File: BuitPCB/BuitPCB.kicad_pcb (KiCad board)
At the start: 2 copper layers, 100 x 100 mm, 46 parts, among them J1 DIN-5_180degree, J10 Conn_01x06, J11 Conn_01x04, J12 Conn_01x04, J13 Conn_01x02, J15 Conn_01x04, J16 Conn_01x04, J2 DIN-5_180degree, J3 USB_A, J4 AudioJack3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

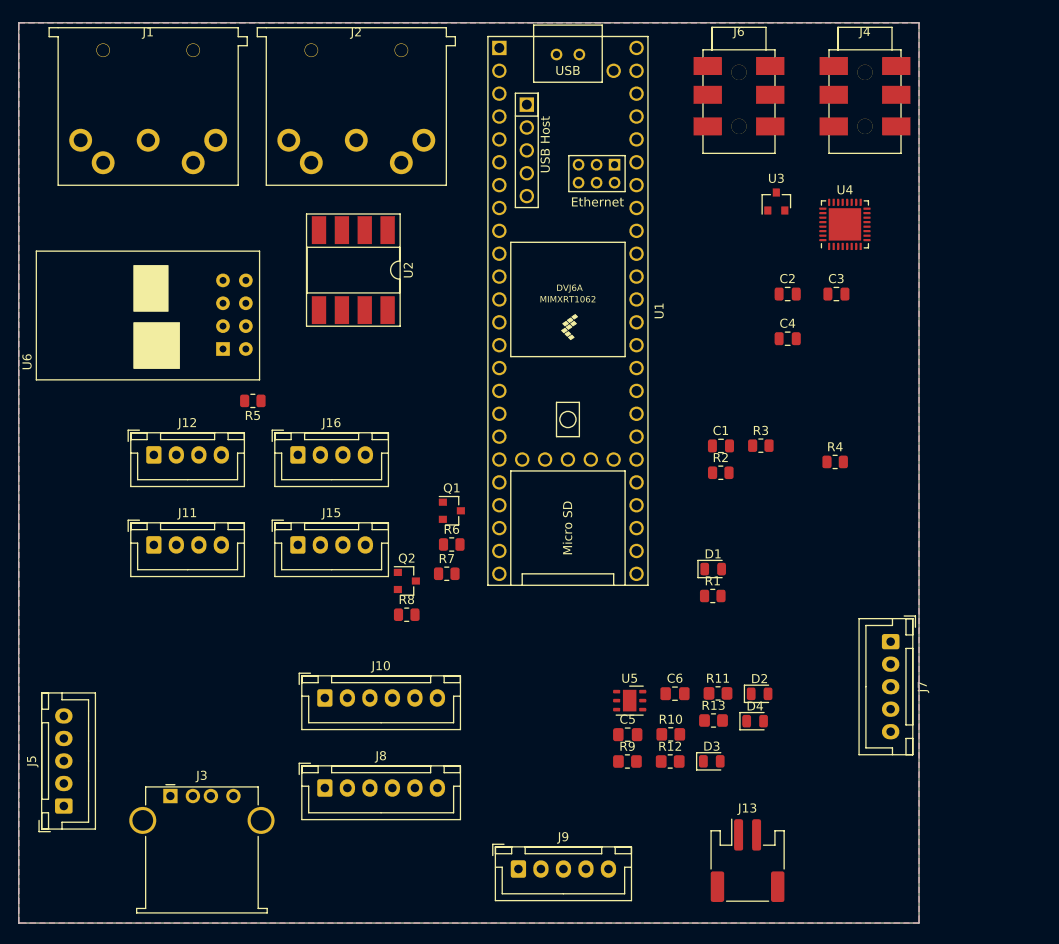
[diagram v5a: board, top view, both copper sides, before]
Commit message: Updated to almost every component and started routing
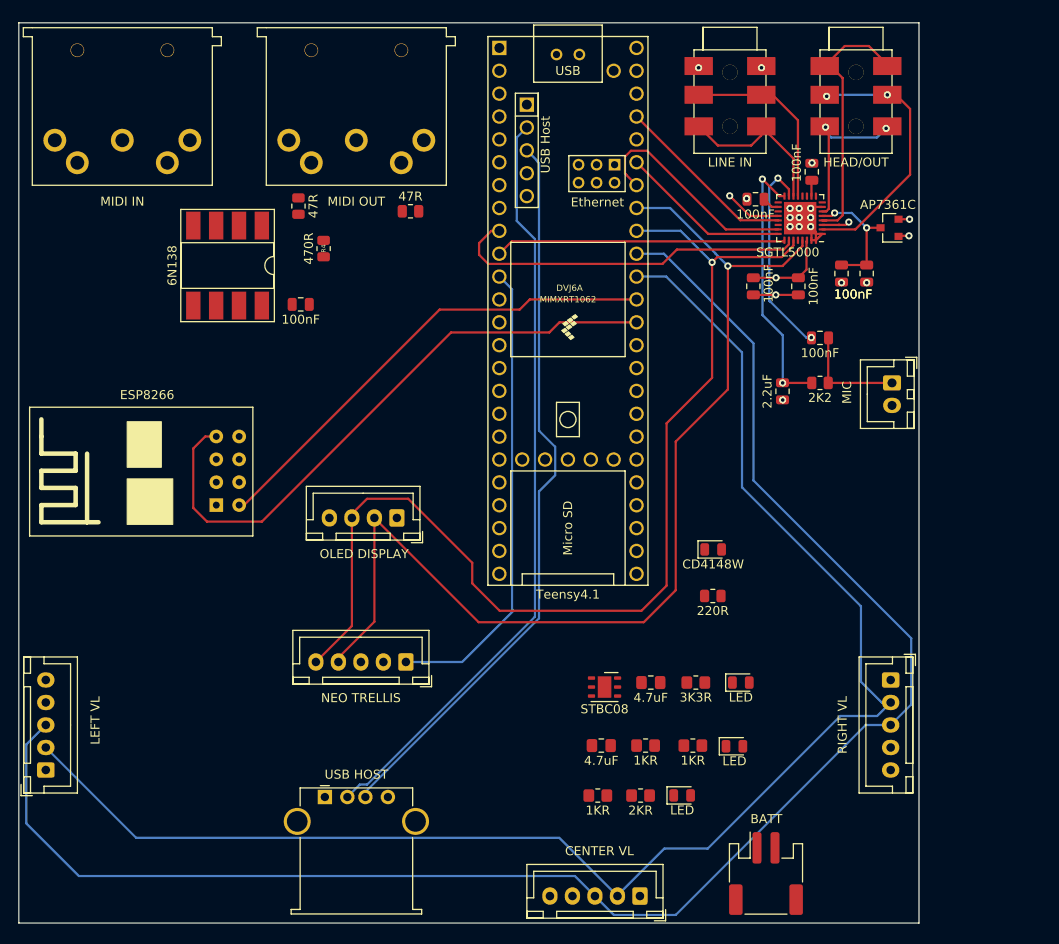
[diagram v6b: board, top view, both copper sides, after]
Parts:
- removed J10: Conn_01x06, Connector_JST:JST_XH_B6B-XH-A_1x06_P2.50mm_Vertical
- removed J15, J16: Conn_01x04, Connector_JST:JST_XH_B4B-XH-A_1x04_P2.50mm_Vertical
- removed Q1, Q2: BSS138, Package_TO_SOT_SMD:SOT-23
- removed R5, R6, R7, R8: 10K, Resistor_SMD:R_0805_2012Metric
- added C10: 100nF, Capacitor_SMD:C_0805_2012Metric, F.Cu at (189.0, 85.0)
- added C11: 2.2uF, Capacitor_SMD:C_0805_2012Metric, F.Cu at (184.8, 90.9)
- added C7: 100nF, Capacitor_SMD:C_0805_2012Metric, F.Cu at (181.6, 79.3)
- added C8: 100nF, Capacitor_SMD:C_0805_2012Metric, F.Cu at (188.1, 66.5)
- added C9: 100nF, Capacitor_SMD:C_0805_2012Metric, F.Cu at (181.8, 69.6)
- added R14: 2K2, Resistor_SMD:R_0805_2012Metric, F.Cu at (189.0, 90.0)
- C1: value C -> 100nF
- J1: value DIN-5_180degree -> MIDI IN
- J11: value Conn_01x04 -> OLED DISPLAY
- J12: value Conn_01x04 -> NEO TRELLIS; footprint Connector_JST:JST_XH_B4B-XH-A_1x04_P2.50mm_Vertical -> Connector_JST:JST_XH_B5B-XH-A_1x05_P2.50mm_Vertical
- J13: value Conn_01x02 -> BATT
- J2: value DIN-5_180degree -> MIDI OUT
- J3: value USB_A -> USB HOST
- J4: value AudioJack3 -> LINE IN
- J5: value LEFT SENS -> LEFT VL
- J6: value AudioJack3 -> HEAD/OUT
- J7: value RIGHT SENS -> RIGHT VL
- J8: value Conn_01x06 -> MIC; footprint Connector_JST:JST_XH_B6B-XH-A_1x06_P2.50mm_Vertical -> Connector_JST:JST_XH_B2B-XH-A_1x02_P2.50mm_Vertical
- J9: value CENTER SENS -> CENTER VL
- U3: value AP7361C-33E -> AP7361C
- U4: value SGTL5000XNAA3 -> SGTL5000
- U6: value ESP82SerialTransc -> ESP8266
- moved J8 77.4 mm to (197.0, 90.0), turned to 270 degrees
- moved R4 61.6 mm to (133.9, 75.1), turned to 270 degrees
- moved R2 55.5 mm to (131.1, 70.4), turned to 90 degrees
- moved C1 49.3 mm to (131.3, 81.3)
- moved R3 46.8 mm to (143.5, 70.9), turned to 180 degrees
- moved J12 36.2 mm to (143.0, 121.0), turned to 180 degrees
- moved J11 27.2 mm to (142.0, 105.0), turned to 180 degrees
- moved U6 17.4 mm to (126.0, 107.0)
- moved J3 17.2 mm to (134.0, 136.0)
- moved J4 15.0 mm to (179.0, 53.0)
- moved U2 14.0 mm to (123.2, 77.0)
- moved J9 13.8 mm to (169.0, 147.0), turned to 180 degrees
- moved J6 13.0 mm to (193.0, 53.0)
- moved U3 12.9 mm to (196.7, 72.8), turned to 180 degrees
- moved C2 6.40 mm to (191.4, 77.9), turned to 270 degrees
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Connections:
- C4 pad 1: Net-(C4-Pad1) -> GND
- C4 pad 2: Net-(C4-Pad2) -> +3V3
- J12 pad 1: +3V3 -> TRELLIS_INT_PIN
- J12 pad 2: I2C_SCL_3V3 -> +3V3
- J12 pad 3: I2C_SDA_3V3 -> GND
- J12 pad 4: GND -> I2C_SCL_3V3
- J8 pad 1: +3V3 -> Net-(C10-Pad2)
- J8 pad 2: SPI_MISO -> GND
- U1 pad 11: Net-(U1-Pad11) -> TRELLIS_INT_PIN
- U4 pad 15: Net-(U4-Pad15) -> MIC
- U4 pad 16: Net-(U4-Pad16) -> MIC_BIAS
- U4 pad 20: Net-(U4-Pad20) -> +3V3
- U4 pad 30: Net-(U4-Pad30) -> +3V3
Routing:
- net SENS_I2C_SDA: track 0.00 -> 188.5 mm
- net SENS_I2C_SCL: track 0.00 -> 171.1 mm
- net I2C_SDA_3V3: track 0.00 -> 119.7 mm, vias 0 -> 1
- net I2C_SCL_3V3: track 0.00 -> 118.5 mm, vias 0 -> 1
- net USB_HOST_D-: track 0.00 -> 84.8 mm
- net USB_HOST_D+: track 0.00 -> 81.9 mm
- net ESP8266_UART_RX: track 0.00 -> 68.8 mm
- net ESP8266_UART_TX: track 0.00 -> 53.6 mm
- net TRELLIS_INT_PIN: track 0.00 -> 52.1 mm
- net I2S_DIN: track 0.00 -> 40.3 mm
- net I2S_DOUT: track 0.00 -> 32.3 mm
- net MIC_BIAS: track 0.00 -> 30.3 mm, vias 0 -> 2
- net HP_GND: track 0.00 -> 29.6 mm
- net HP_R: track 0.00 -> 29.6 mm, vias 0 -> 2
- net I2S_LRCLK: track 0.00 -> 24.6 mm
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- added copper zone on In2.Cu, net +3V3
- added copper zone on In1.Cu, net GND
- removed copper zone on B.Cu, net GND
- removed copper zone on F.Cu, net GND
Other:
- copper layers 2 -> 4

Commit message: Added drills on pcb
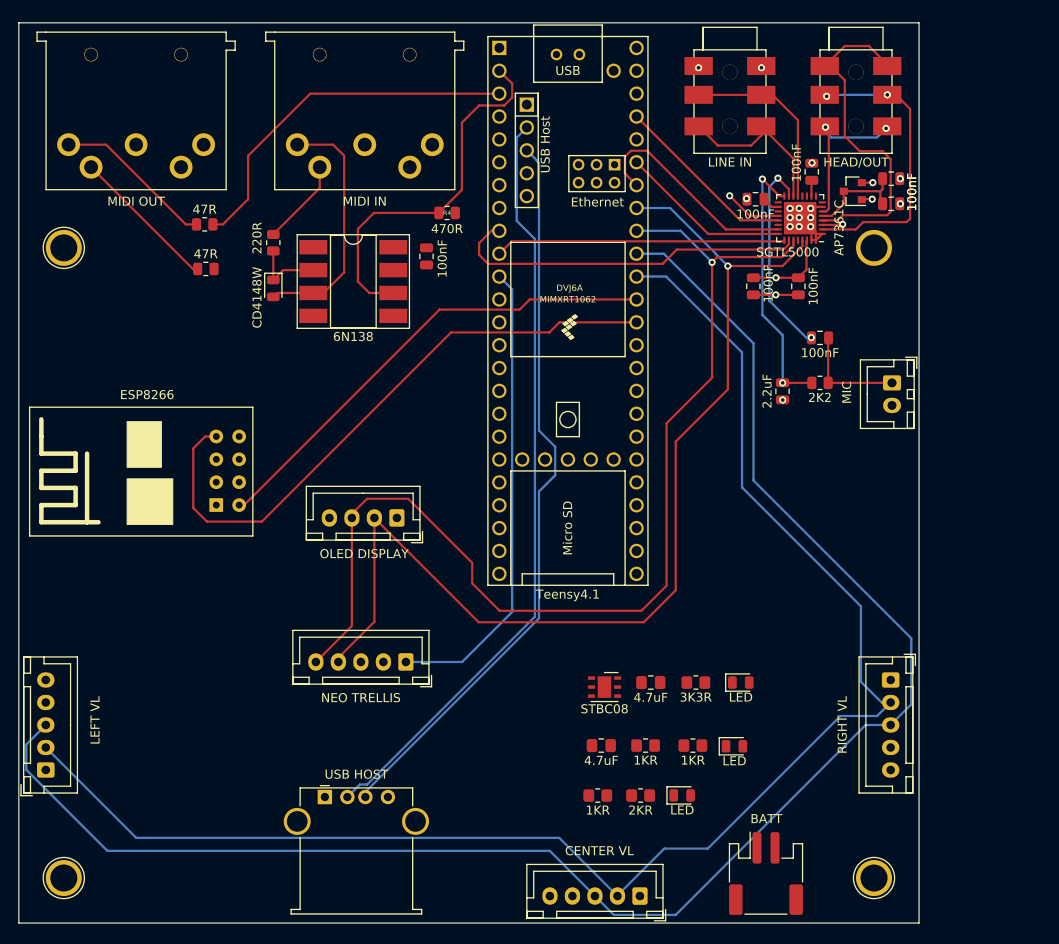
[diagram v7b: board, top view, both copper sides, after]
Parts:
- added ?: , , F.Cu at (195.0, 75.0)
- added REF**: TestPoint_Plated_Hole_D3.0mm, TestPoint:TestPoint_Plated_Hole_D3.0mm, F.Cu at (195.0, 145.0)
- added REF**: TestPoint_Plated_Hole_D3.0mm, TestPoint:TestPoint_Plated_Hole_D3.0mm, F.Cu at (105.0, 145.0)
- added REF**: TestPoint_Plated_Hole_D3.0mm, TestPoint:TestPoint_Plated_Hole_D3.0mm, F.Cu at (105.0, 75.0)
- moved R1 62.6 mm to (128.3, 74.4), turned to 90 degrees
- moved D1 56.8 mm to (128.3, 79.5), turned to -90 degrees
- moved J1 26.9 mm to (138.4, 51.0)
- moved J2 24.5 mm to (113.0, 51.0)
- moved R3 22.9 mm to (120.7, 72.4)
- moved C1 15.0 mm to (145.3, 75.9), turned to -90 degrees
- moved R4 14.3 mm to (147.6, 71.1), turned to 180 degrees
- moved U2 14.1 mm to (137.2, 78.7), turned to 0 degrees
- moved R2 12.4 mm to (120.8, 77.3), turned to 180 degrees
- moved C3 10.9 mm to (196.9, 67.3), turned to 0 degrees
- moved C2 9.51 mm to (196.9, 70.1), turned to 0 degrees
- moved U3 5.76 mm to (192.6, 68.7)
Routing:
- net MIDI_IN: track 0.00 -> 41.4 mm
- net MIDI_OUT: track 0.00 -> 40.7 mm
- net Net-(D1-Pad2): track 0.00 -> 27.7 mm
- net Net-(J2-Pad5): track 0.00 -> 17.9 mm
- net Net-(J2-Pad4): track 0.00 -> 16.5 mm
- net Net-(J1-Pad4): track 0.00 -> 9.61 mm
- net HP_GND: track 29.6 -> 38.4 mm
- net Net-(D1-Pad1): track 0.00 -> 8.13 mm
- net SENS_I2C_SDA: track 188.5 -> 185.0 mm
- net HP_R: track 29.6 -> 32.4 mm
- net VDDA: track 14.2 -> 11.4 mm, vias 2 -> 0
- net GND: track 18.8 -> 17.5 mm
- removed copper zone on In2.Cu, net +3V3
- removed copper zone on In1.Cu, net GND
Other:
- net class Default removed

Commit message: Updated almost to final 0.1 version
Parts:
- removed D2, D3, D4: LED, LED_SMD:LED_0805_2012Metric
- removed J13: BATT, Connector_JST:JST_PH_S2B-PH-SM4-TB_1x02-1MP_P2.00mm_Horizontal
- removed R10, R13, R9: 1KR, Resistor_SMD:R_0805_2012Metric_Pad1.20x1.40mm_HandSolder
- removed R11: 3K3R, Resistor_SMD:R_0805_2012Metric_Pad1.20x1.40mm_HandSolder
- removed R12: 2KR, Resistor_SMD:R_0805_2012Metric_Pad1.20x1.40mm_HandSolder
- removed the REF** at (195.0, 145.0)
- removed the REF** at (105.0, 75.0)
- removed U5: STBC08, Package_DFN_QFN:DFN-6-1EP_3x3mm_P1mm_EP1.5x2.4mm
- added ?: , , F.Cu at (105.0, 75.0)
- added ?: , , F.Cu at (195.0, 145.0)
- added C12: 100nF, Capacitor_SMD:C_0805_2012Metric, F.Cu at (146.4, 78.3)
- added J10: ROTARY CLICK, Connector_JST:JST_XH_B5B-XH-A_1x05_P2.50mm_Vertical, F.Cu at (133.3, 92.8)
- added R5: 3K3, Resistor_SMD:R_0805_2012Metric, F.Cu at (177.6, 92.9)
- added R6: 3K3, Resistor_SMD:R_0805_2012Metric, F.Cu at (175.5, 90.1)
- added R7: 3K3, Resistor_SMD:R_0805_2012Metric, F.Cu at (179.1, 99.4)
- added R8: 3K3, Resistor_SMD:R_0805_2012Metric, F.Cu at (182.8, 99.4)
- C5, C6: value 4.7uF -> 100nF; footprint Capacitor_SMD:C_0805_2012Metric_Pad1.18x1.45mm_HandSolder -> Capacitor_SMD:C_0805_2012Metric
- D1: value CD4148W -> 1N4148
- moved C6 53.9 mm to (146.4, 74.9), turned to 180 degrees
- moved C5 52.0 mm to (146.4, 81.6), turned to 180 degrees
- moved U6 6.85 mm to (125.7, 100.2)
- moved C1 4.59 mm to (142.6, 72.2), turned to 0 degrees
- moved U1 0.14 mm to (160.9, 82.1)
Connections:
- net USB_HOST_D+ renamed USB_HOST_P
- net USB_HOST_D- renamed USB_HOST_N
- C1 pad 1: +5V -> V_USB
- C5 pad 1: V_USB -> GND
- C5 pad 2: GND -> V_USB
- C6 pad 1: V_BAT -> GND
- C6 pad 2: GND -> V_USB
- J1 pad 1: Net-(J1-Pad1) -> unconnected-(J1-Pad1)
- J1 pad 2: Net-(J1-Pad2) -> unconnected-(J1-Pad2)
- J1 pad 3: Net-(J1-Pad3) -> unconnected-(J1-Pad3)
- J2 pad 1: Net-(J2-Pad1) -> unconnected-(J2-Pad1)
- J2 pad 2: Net-(J2-Pad2) -> unconnected-(J2-Pad2)
- J2 pad 3: Net-(J2-Pad3) -> unconnected-(J2-Pad3)
- J3 pad 1: Net-(J3-Pad1) -> USB_HOST_5V
- U1 pad 12: Net-(U1-Pad12) -> ROT_CLICK_SW
- U1 pad 13: Net-(U1-Pad13) -> ROT_CLICK_DT
- U1 pad 14: Net-(U1-Pad14) -> ROT_CLICK_CLK
- U1 pad 16: Net-(U1-Pad16) -> unconnected-(U1-Pad16)
- U1 pad 17: Net-(U1-Pad17) -> unconnected-(U1-Pad17)
- U1 pad 18: Net-(U1-Pad18) -> unconnected-(U1-Pad18)
- U1 pad 19: Net-(U1-Pad19) -> unconnected-(U1-Pad19)
- U1 pad 20: Net-(U1-Pad20) -> unconnected-(U1-Pad20)
- U1 pad 21: Net-(U1-Pad21) -> unconnected-(U1-Pad21)
- U1 pad 22: Net-(U1-Pad22) -> unconnected-(U1-Pad22)
- U1 pad 23: Net-(U1-Pad23) -> unconnected-(U1-Pad23)
- U1 pad 24: Net-(U1-Pad24) -> unconnected-(U1-Pad24)
- U1 pad 25: Net-(U1-Pad25) -> unconnected-(U1-Pad25)
- U1 pad 26: Net-(U1-Pad26) -> unconnected-(U1-Pad26)
- U1 pad 27: Net-(U1-Pad27) -> unconnected-(U1-Pad27)
- U1 pad 28: Net-(U1-Pad28) -> unconnected-(U1-Pad28)
- U1 pad 29: Net-(U1-Pad29) -> unconnected-(U1-Pad29)
- U1 pad 30: Net-(U1-Pad30) -> unconnected-(U1-Pad30)
- U1 pad 31: Net-(U1-Pad31) -> unconnected-(U1-Pad31)
- U1 pad 32: Net-(U1-Pad32) -> unconnected-(U1-Pad32)
- U1 pad 33: Net-(U1-Pad33) -> unconnected-(U1-Pad33)
- U1 pad 35: Net-(U1-Pad35) -> unconnected-(U1-Pad35)
- U1 pad 44: Net-(U1-Pad44) -> unconnected-(U1-Pad44)
- U1 pad 46: Net-(U1-Pad46) -> +3V3
- U1 pad 48: Net-(U1-Pad48) -> V_USB
- U1 pad 49: V_USB -> unconnected-(U1-Pad49)
- U1 pad 50: Net-(U1-Pad50) -> unconnected-(U1-Pad50)
- U1 pad 53: Net-(U1-Pad53) -> unconnected-(U1-Pad53)
- U1 pad 54: Net-(U1-Pad54) -> unconnected-(U1-Pad54)
- U1 pad 60: Net-(U1-Pad60) -> unconnected-(U1-Pad60)
- U1 pad 61: Net-(U1-Pad61) -> unconnected-(U1-Pad61)
- U1 pad 62: Net-(U1-Pad62) -> unconnected-(U1-Pad62)
- U1 pad 63: Net-(U1-Pad63) -> unconnected-(U1-Pad63)
- U1 pad 65: Net-(U1-Pad65) -> unconnected-(U1-Pad65)
- U1 pad 66: Net-(U1-Pad66) -> unconnected-(U1-Pad66)
- U1 pad 67: Net-(U1-Pad67) -> unconnected-(U1-Pad67)
- U1 pad 7: Net-(U1-Pad7) -> unconnected-(U1-Pad7)
- U1 pad 8: Net-(U1-Pad8) -> unconnected-(U1-Pad8)
- U2 pad 1: Net-(U2-Pad1) -> unconnected-(U2-Pad1)
- U2 pad 4: Net-(U2-Pad4) -> unconnected-(U2-Pad4)
- U2 pad 7: Net-(U2-Pad7) -> unconnected-(U2-Pad7)
- U2 pad 8: +5V -> V_USB
- U4 pad 17: Net-(U4-Pad17) -> unconnected-(U4-Pad17)
- U4 pad 19: Net-(U4-Pad19) -> unconnected-(U4-Pad19)
- U4 pad 22: Net-(U4-Pad22) -> unconnected-(U4-Pad22)
- U4 pad 28: Net-(U4-Pad28) -> unconnected-(U4-Pad28)
- U4 pad 8: Net-(U4-Pad8) -> unconnected-(U4-Pad8)
- U4 pad 9: Net-(U4-Pad9) -> unconnected-(U4-Pad9)
- U6 pad 2: Net-(U6-Pad2) -> unconnected-(U6-Pad2)
- U6 pad 3: Net-(U6-Pad3) -> unconnected-(U6-Pad3)
- U6 pad 6: Net-(U6-Pad6) -> unconnected-(U6-Pad6)
- U6 pad 7: Net-(U6-Pad7) -> unconnected-(U6-Pad7)
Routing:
- net USB_HOST_5V: track 0.00 -> 157.3 mm
- net SENS_XOUT_RIGHT: track 0.00 -> 136.1 mm, vias 0 -> 1
- net SENS_XOUT_CENTER: track 0.00 -> 112.5 mm, vias 0 -> 1
- net SENS_XOUT_LEFT: track 0.00 -> 86.0 mm
- net V_USB: track 0.00 -> 60.4 mm, vias 0 -> 1
- net ROT_CLICK_SW: track 0.00 -> 20.1 mm
- net ROT_CLICK_DT: track 0.00 -> 16.5 mm
- net ROT_CLICK_CLK: track 0.00 -> 13.0 mm
- net ESP8266_UART_RX: track 68.8 -> 56.8 mm
- net USB_HOST_P: track 81.9 -> 87.3 mm
- net USB_HOST_N: track 84.8 -> 87.4 mm
- net ESP8266_UART_TX: track 53.6 -> 51.1 mm
- net +3V3: track 17.1 -> 16.2 mm, vias 3 -> 9
- net GND: track 17.5 -> 17.1 mm, vias 19 -> 23
- net SENS_I2C_SDA: track 185.0 -> 184.7 mm, vias 0 -> 1
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- added copper zone on In2.Cu, net +3V3
- added copper zone on In1.Cu, net GND
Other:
- board text added: "BUÏT"
- board text added: "board v0.1"
- board text added: "by RTP"
